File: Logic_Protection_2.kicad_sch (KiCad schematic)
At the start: 15 parts

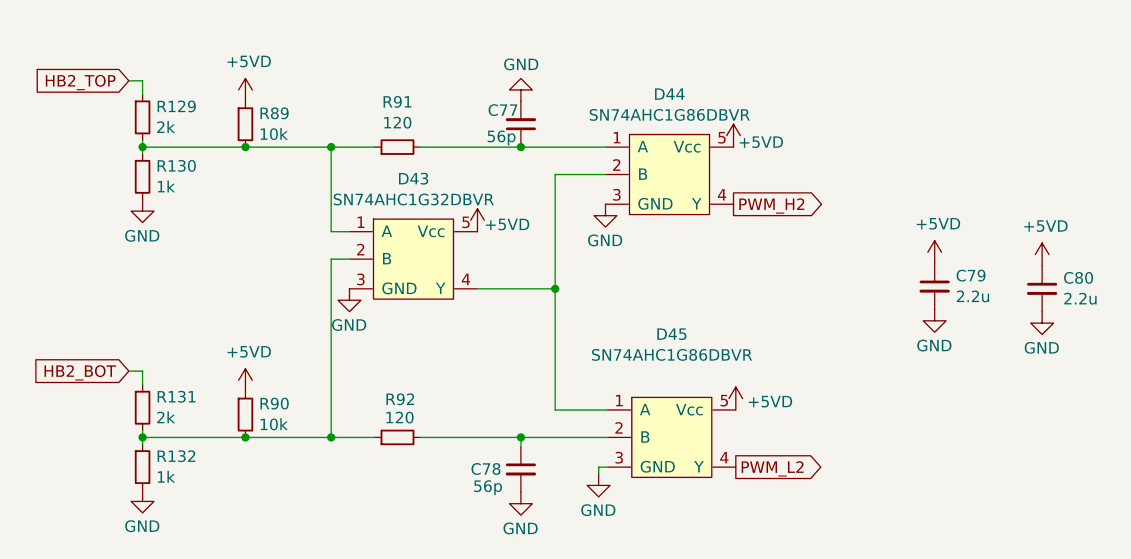
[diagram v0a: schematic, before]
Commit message: Всё влезло, осталься компаратор на NTC
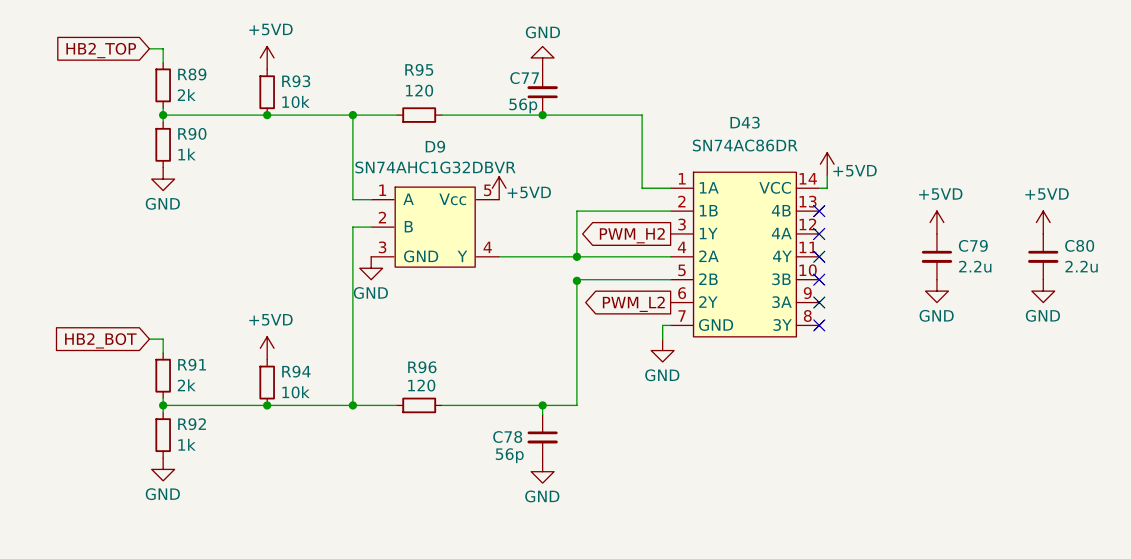
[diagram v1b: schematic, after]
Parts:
- removed D43: SN74AHC1G32DBVR, Package_TO_SOT_SMD:SOT-23-5_HandSoldering, symbol Logic:SN74AHC1G86DBVR
- removed D44, D45: SN74AHC1G86DBVR, Package_TO_SOT_SMD:SOT-23-5_HandSoldering, symbol Logic:SN74AHC1G86DBVR
- removed R129, R131: 2k, Resistor_SMD:R_0805_2012Metric_Pad1.20x1.40mm_HandSolder, symbol Device:R_Small
- removed R130, R132: 1k, Resistor_SMD:R_0805_2012Metric_Pad1.20x1.40mm_HandSolder, symbol Device:R_Small
- added D43: SN74AC86DR, Package_SO:SOIC-14_3.9x8.7mm_P1.27mm, symbol Logic_My:SN74AC86DR
- added D9: SN74AHC1G32DBVR, Package_TO_SOT_SMD:SOT-23-5_HandSoldering, symbol Logic:SN74AHC1G86DBVR
- added R93, R94: 10k, Resistor_SMD:R_0805_2012Metric_Pad1.20x1.40mm_HandSolder, symbol Device:R_Small
- added R95, R96: 120, Resistor_SMD:R_0805_2012Metric_Pad1.20x1.40mm_HandSolder, symbol Device:R_Small
- R89: value 10k -> 2k
- R90: value 10k -> 1k
- R91: value 120 -> 2k
- R92: value 120 -> 1k
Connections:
- net +5VD: now also D43.14 (VCC), D9.5 (Vcc), R93.1, R94.1; no longer R89.1, R90.1
- net GND: now also R90.2, R92.2, D43.7 (GND), D9.3 (GND)
- net HB2_BOT: now also R91.1
- net HB2_TOP: now also R89.1
- net PWM_H2: now also D43.3 (1Y)
- net PWM_L2: now also D43.6 (2Y)
- net at R89.2: now also R90.1, D9.1 (A), R93.2, R95.1; no longer R91.1
- net at R92.1: now also R91.2, D9.2 (B), R94.2, R96.1; no longer R90.2
- net at C77.1: now also D43.1 (1A), R95.2; no longer R91.2
- net at C78.1: now also D43.5 (2B), R96.2; no longer R92.2
- new net: D43.2 (1B), D43.4 (2A), D9.4 (Y)
- no-connect marks 0 -> 6

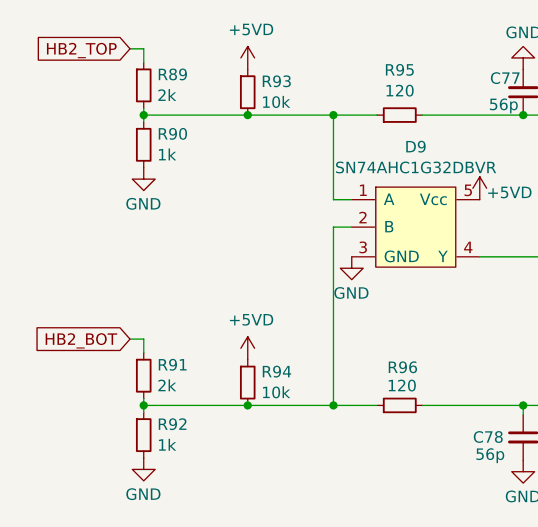
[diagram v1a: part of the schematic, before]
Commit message: Исправил ошибки, добавил резисторы в затвор, ревизия 2.0
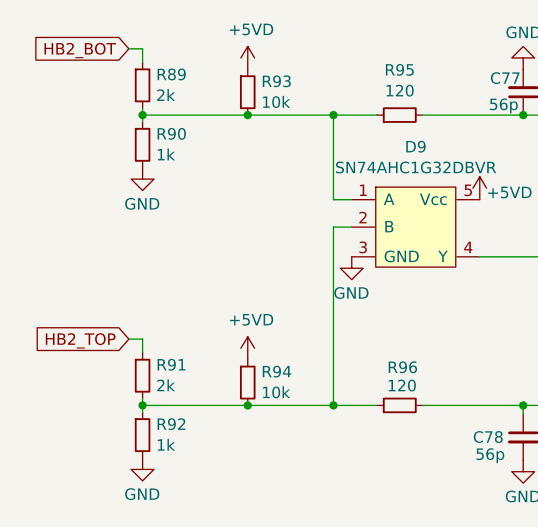
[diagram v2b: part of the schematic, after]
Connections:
- net HB2_BOT: now also R89.1; no longer R91.1
- net HB2_TOP: now also R91.1; no longer R89.1

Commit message: Версия для резонита REV2.1
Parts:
- removed C77, C78: 56p, Capacitor_SMD:C_0805_2012Metric_Pad1.18x1.45mm_HandSolder, symbol Device:C_Small
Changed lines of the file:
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@@
   (junction (at 122.809 112.014) (diameter 0) (color 0 0 0 0)
-  )
-  (junction (at 143.891 112.014) (diameter 0) (color 0 0 0 0)
   )
   (junction (at 101.6 79.756) (diameter 0) (color 0 0 0 0)
@@
   )
   (junction (at 101.6 112.014) (diameter 0) (color 0 0 0 0)
-  )
-  (junction (at 143.891 79.756) (diameter 0) (color 0 0 0 0)
   )
   (junction (at 147.701 95.504) (diameter 0) (color 0 0 0 0)
@@
     (stroke (width 0) (type default) (color 0 0 0 0))
   )
-  (wire (pts (xy 147.701 112.014) (xy 143.891 112.014))
+  (wire (pts (xy 132.715 112.014) (xy 147.701 112.014))
     (stroke (width 0) (type default) (color 0 0 0 0))
   )
-  (wire (pts (xy 132.715 79.756) (xy 143.891 79.756))
+  (wire (pts (xy 132.715 79.756) (xy 154.94 79.756))
     (stroke (width 0) (type default) (color 0 0 0 0))
   )
   (wire (pts (xy 124.841 92.202) (xy 122.809 92.202))
-    (stroke (width 0) (type default) (color 0 0 0 0))
-  )
-  (wire (pts (xy 143.891 112.014) (xy 143.891 113.03))
     (stroke (width 0) (type default) (color 0 0 0 0))
   )
@@
   )
   (wire (pts (xy 101.6 112.014) (xy 113.284 112.014))
-    (stroke (width 0) (type default) (color 0 0 0 0))
-  )
-  (wire (pts (xy 143.891 79.756) (xy 154.94 79.756))
     (stroke (width 0) (type default) (color 0 0 0 0))
   )
@@
   )
   (wire (pts (xy 175.514 87.884) (xy 174.625 87.884))
-    (stroke (width 0) (type default) (color 0 0 0 0))
-  )
-  (wire (pts (xy 132.715 112.014) (xy 143.891 112.014))
     (stroke (width 0) (type default) (color 0 0 0 0))
   )
@@
       (effects (font (size 1.27 1.27)) hide)
     )
-    (pin "1")
-  )
-  (symbol (lib_id "Device:C_Small") (at 143.891 77.216 180) (unit 1)
-    (in_bom yes) (on_board yes)
-    (property "Reference" "C77" (id 0) (at 143.637 75.692 0)
-      (effects (font (size 1.27 1.27)) (justify left))
-    )
-    (property "Value" "56p" (id 1) (at 143.383 78.613 0)
-      (effects (font (size 1.27 1.27)) (justify left))
-    )
-    (property "Footprint" "Capacitor_SMD:C_0805_2012Metric_Pad1.18x1.45mm_HandSolder" (id 2) (at 143.891 77.216 0)
-      (effects (font (size 1.27 1.27)) hide)
-    )
-    (property "Datasheet" "~" (id 3) (at 143.891 77.216 0)
-      (effects (font (size 1.27 1.27)) hide)
-    )
-    (pin "1")
-    (pin "2")
-  )
-  (symbol (lib_id "Device:C_Small") (at 143.891 115.57 0) (unit 1)
-    (in_bom yes) (on_board yes)
-    (property "Reference" "C78" (id 0) (at 138.303 115.57 0)
-      (effects (font (size 1.27 1.27)) (justify left))
-    )
-    (property "Value" "56p" (id 1) (at 138.557 117.475 0)
-      (effects (font (size 1.27 1.27)) (justify left))
-    )
-    (property "Footprint" "Capacitor_SMD:C_0805_2012Metric_Pad1.18x1.45mm_HandSolder" (id 2) (at 143.891 115.57 0)
-      (effects (font (size 1.27 1.27)) hide)
-    )
-    (property "Datasheet" "~" (id 3) (at 143.891 115.57 0)
-      (effects (font (size 1.27 1.27)) hide)
-    )
-    (pin "1")
-    (pin "2")
-  )
-  (symbol (lib_id "power:GND") (at 143.891 74.676 180) (unit 1)
-    (in_bom yes) (on_board yes)
-    (property "Reference" "#PWR043" (id 0) (at 143.891 68.326 0)
-      (effects (font (size 1.27 1.27)) hide)
-    )
-    (property "Value" "GND" (id 1) (at 145.923 70.612 0)
-      (effects (font (size 1.27 1.27)) (justify left))
-    )
-    (property "Footprint" "" (id 2) (at 143.891 74.676 0)
-      (effects (font (size 1.27 1.27)) hide)
-    )
-    (property "Datasheet" "" (id 3) (at 143.891 74.676 0)
-      (effects (font (size 1.27 1.27)) hide)
-    )
-    (pin "1")
-  )
-  (symbol (lib_id "power:GND") (at 143.891 118.11 0) (unit 1)
-    (in_bom yes) (on_board yes)
-    (property "Reference" "#PWR044" (id 0) (at 143.891 124.46 0)
-      (effects (font (size 1.27 1.27)) hide)
-    )
-    (property "Value" "GND" (id 1) (at 141.859 122.174 0)
-      (effects (font (size 1.27 1.27)) (justify left))
-    )
-    (property "Footprint" "" (id 2) (at 143.891 118.11 0)
-      (effects (font (size 1.27 1.27)) hide)
-    )
-    (property "Datasheet" "" (id 3) (at 143.891 118.11 0)
-      (effects (font (size 1.27 1.27)) hide)
-    )
